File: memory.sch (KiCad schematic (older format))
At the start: 11 parts, among them U21 sst39x040, U22 generic_2048x8_TSOP_II_44, U23 generic_2048x8_TSOP_II_44, U24 generic_2048x8_TSOP_II_44, U25 generic_2048x8_TSOP_II_44

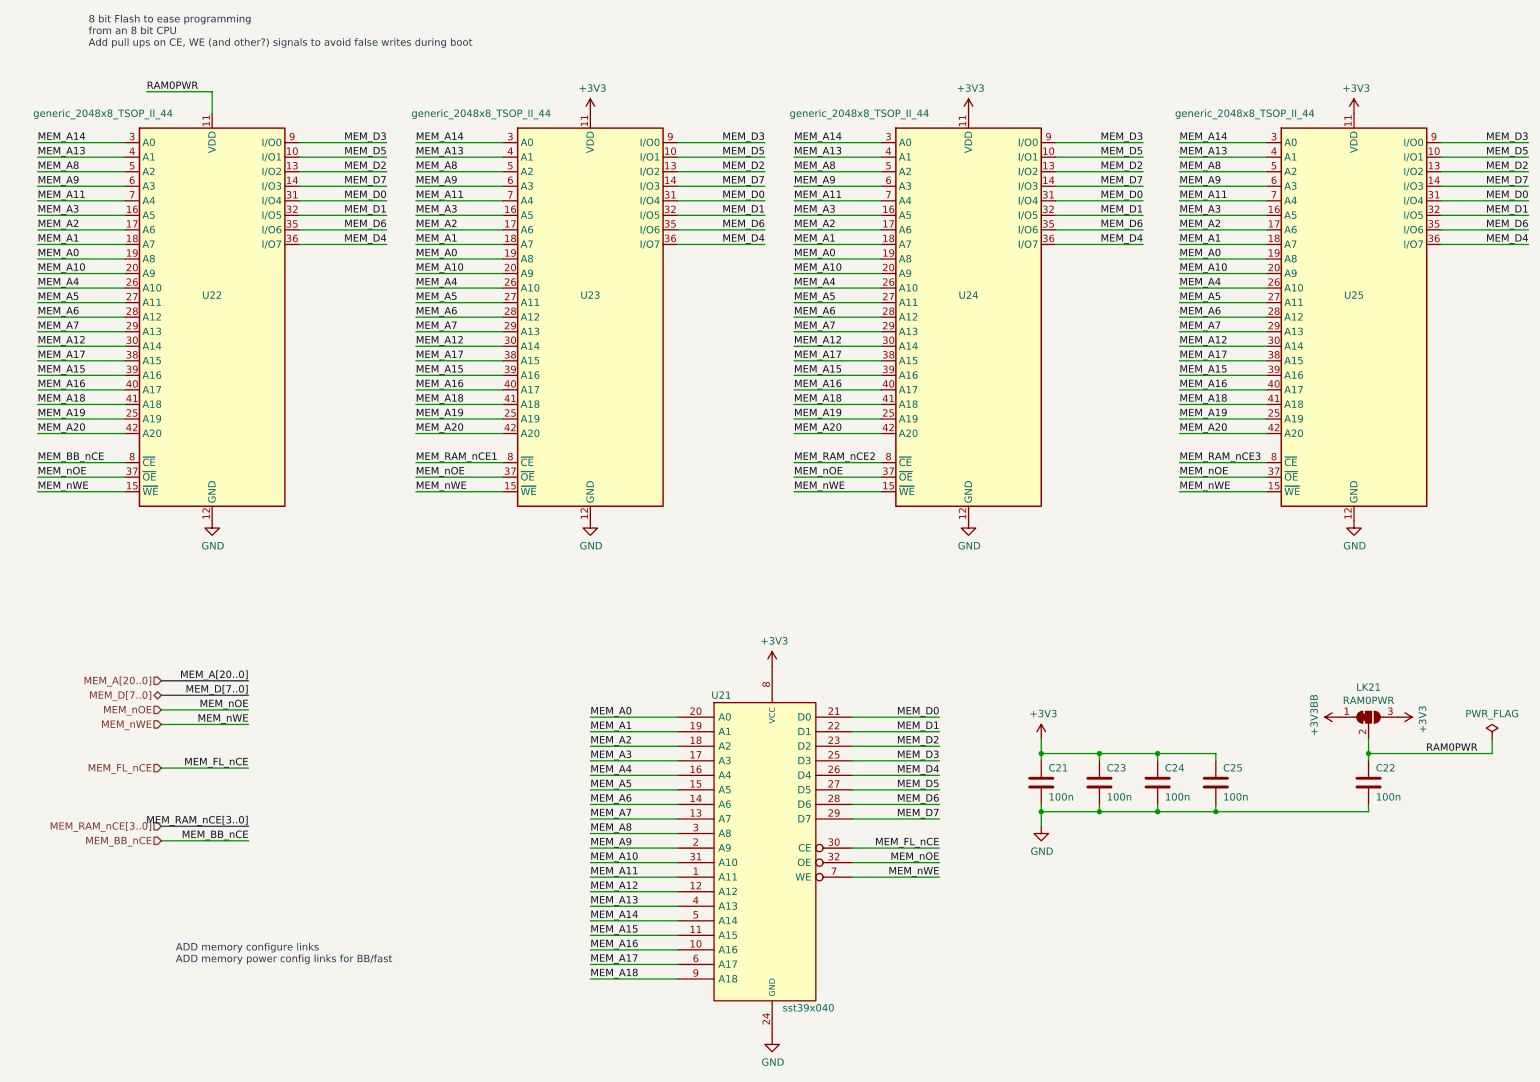
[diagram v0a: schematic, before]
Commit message: Mk.3 fixes and new 68000 expansion board
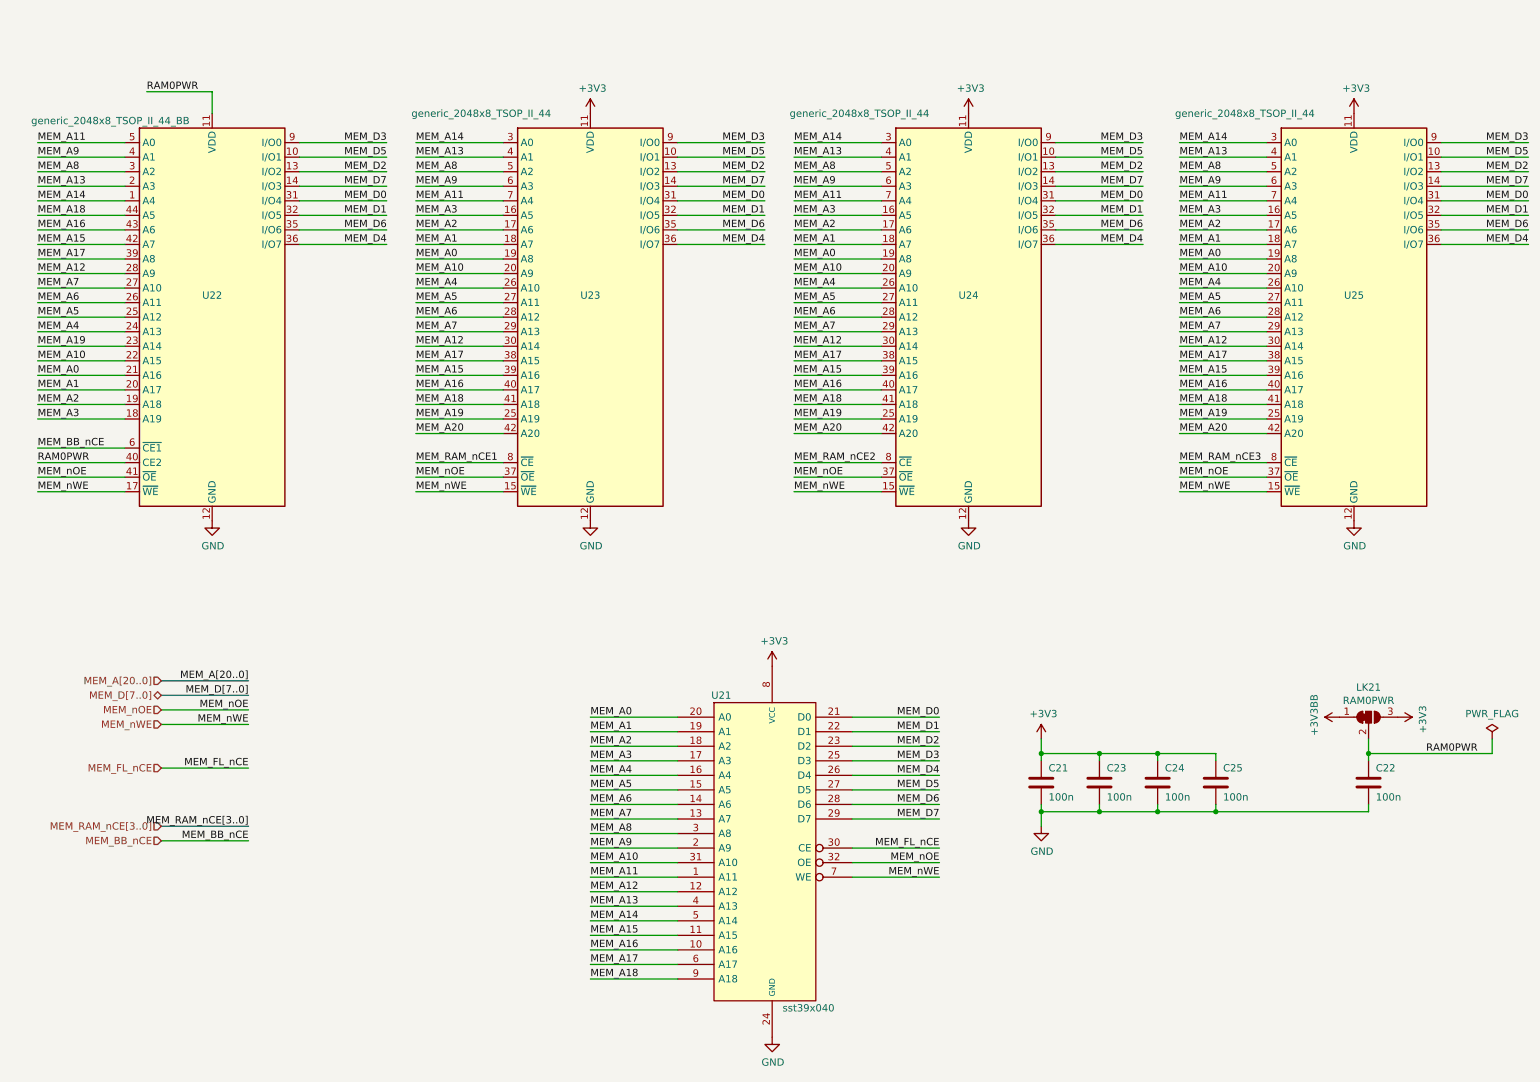
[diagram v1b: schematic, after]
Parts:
- removed U22: generic_2048x8_TSOP_II_44, Package_SO:TSOP-II-44_10.16x18.41mm_P0.8mm, symbol memory:generic_2048x8_TSOP_II_44
- added U22: generic_2048x8_TSOP_II_44_BB, Package_SO:TSOP-II-44_10.16x18.41mm_P0.8mm, symbol memory:generic_2048x8_TSOP_II_44_BB
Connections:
- net GND: now also U22.12 (GND), U22.34 (GND)
- net MEM_A0: now also U22.21 (A16)
- net MEM_A1: now also U22.20 (A17)
- net MEM_A10: now also U22.22 (A15)
- net MEM_A11: now also U22.5 (A0)
- net MEM_A12: now also U22.28 (A9)
- net MEM_A13: now also U22.2 (A3)
- net MEM_A14: now also U22.1 (A4)
- net MEM_A15: now also U22.42 (A7)
- net MEM_A16: now also U22.43 (A6)
- net MEM_A17: now also U22.39 (A8)
- net MEM_A18: now also U22.44 (A5)
- net MEM_A19: now also U22.23 (A14)
- net MEM_A2: now also U22.19 (A18)
- net MEM_A3: now also U22.18 (A19)
- net MEM_A4: now also U22.24 (A13)
- net MEM_A5: now also U22.25 (A12)
- net MEM_A6: now also U22.26 (A11)
- net MEM_A7: now also U22.27 (A10)
- net MEM_A8: now also U22.3 (A2)
- net MEM_A9: now also U22.4 (A1)
- net MEM_BB_nCE: now also U22.6 (~CE1)
- net MEM_D0: now also U22.31 (I/O4)
- net MEM_D1: now also U22.32 (I/O5)
- net MEM_D2: now also U22.13 (I/O2)
- net MEM_D3: now also U22.9 (I/O0)
- net MEM_D4: now also U22.36 (I/O7)
- net MEM_D5: now also U22.10 (I/O1)
- net MEM_D6: now also U22.35 (I/O6)
- net MEM_D7: now also U22.14 (I/O3)
- net MEM_nOE: now also U22.41 (~OE)
- net MEM_nWE: now also U22.17 (~WE)
- net RAM0PWR: now also U22.11 (VDD), U22.33 (VDD), U22.40 (CE2)
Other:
- note removed: "8 bit Flash to ease programming\nfrom an 8 bit CPU\nAdd pull ups on CE, WE (and other?) signals to avoid false writes during boot"
- note removed: "ADD memory configure links\nADD memory power config links for BB/fast"
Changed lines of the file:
@@
 Sheet 3 11
 Title "Mk.3 Blitter FPGA development board"
-Date "2021-05-08"
-Rev "3.00"
+Date "2021-08-14"
+Rev "3.03"
 Comp "Dossytronics"
-Comment1 ""
+Comment1 "fixed: clk/sysd0, jtag, u22 footprint"
 Comment2 ""
 Comment3 ""
 Comment4 ""
 $EndDescr
-Text Notes 950  800  0    50   ~ 0
-8 bit Flash to ease programming\nfrom an 8 bit CPU\nAdd pull ups on CE, WE (and other?) signals to avoid false writes during boot
 $Comp
 L sst39:sst39x040 U21
@@
 Text Label 6800 6100 2    50   ~ 0
 MEM_D7
-Text Label 600  2150 0    50   ~ 0
+Text Label 600  3150 0    50   ~ 0
 MEM_A1
-Text Label 600  2050 0    50   ~ 0
+Text Label 600  3250 0    50   ~ 0
 MEM_A2
-Text Label 600  1950 0    50   ~ 0
+Text Label 600  3350 0    50   ~ 0
 MEM_A3
+Text Label 600  2750 0    50   ~ 0
+MEM_A4
+Text Label 600  2650 0    50   ~ 0
+MEM_A5
+Text Label 600  2550 0    50   ~ 0
+MEM_A6
 Text Label 600  2450 0    50   ~ 0
-MEM_A4
-Text Label 600  2550 0    50   ~ 0
-MEM_A5
-Text Label 600  2650 0    50   ~ 0
-MEM_A6
-Text Label 600  2750 0    50   ~ 0
 MEM_A7
 Text Label 600  1650 0    50   ~ 0
 MEM_A8
+Text Label 600  1550 0    50   ~ 0
+MEM_A9
+Text Label 600  2950 0    50   ~ 0
+MEM_A10
+Text Label 600  1450 0    50   ~ 0
+MEM_A11
+Text Label 600  2350 0    50   ~ 0
+MEM_A12
 Text Label 600  1750 0    50   ~ 0
-MEM_A9
-Text Label 600  2350 0    50   ~ 0
-MEM_A10
+MEM_A13
 Text Label 600  1850 0    50   ~ 0
-MEM_A11
-Text Label 600  2850 0    50   ~ 0
-MEM_A12
-Text Label 600  1550 0    50   ~ 0
-MEM_A13
-Text Label 600  1450 0    50   ~ 0
 MEM_A14
-Text Label 600  2950 0    50   ~ 0
+Text Label 600  2250 0    50   ~ 0
 MEM_A17
-Text Label 600  3250 0    50   ~ 0
+Text Label 600  1950 0    50   ~ 0
 MEM_A18
 Wire Wire Line
@@
 Wire Wire Line
 	600  3350 1200 3350
-Wire Wire Line
-	600  3450 1200 3450
-Text Label 600  3350 0    50   ~ 0
+Text Label 600  2850 0    50   ~ 0
 MEM_A19
-Text Label 600  3450 0    50   ~ 0
-MEM_A20
-Text Label 600  2250 0    50   ~ 0
+Text Label 600  3050 0    50   ~ 0
 MEM_A0
-Text Notes 1550 7100 0    50   ~ 0
-ADD memory configure links\nADD memory power config links for BB/fast
-$Comp
-L memory:generic_2048x8_TSOP_II_44 U22
-U 1 1 60D1BD24
-P 1800 2550
-F 0 "U22" H 1800 2600 50  0000 C CNN
-F 1 "generic_2048x8_TSOP_II_44" H 1050 3850 50  0000 C CNN
-F 2 "Package_SO:TSOP-II-44_10.16x18.41mm_P0.8mm" H 750 3900 50  0001 C CNN
-F 3 "http://www.issi.com/WW/pdf/61-64C5128AL.pdf" H 1800 2550 50  0001 C CNN
-	1    1800 2550
-	1    0    0    -1
-$EndComp
 $Comp
 L power:GND #PWR0138
@@
 Wire Wire Line
 	600  2950 1200 2950
-Text Label 600  3150 0    50   ~ 0
+Text Label 600  2050 0    50   ~ 0
 MEM_A16
-Text Label 600  3050 0    50   ~ 0
+Text Label 600  2150 0    50   ~ 0
 MEM_A15
 Text Label 3200 2150 0    50   ~ 0
@@
 Wire Wire Line
 	9750 5650 10600 5650
-Text Label 600  3650 0    50   ~ 0
+Text Label 600  3550 0    50   ~ 0
 MEM_BB_nCE
 Text Label 2050 6250 2    50   ~ 0
@@
 Text HLabel 1450 6250 0    50   Input ~ 0
 MEM_BB_nCE
+$Comp
+L memory:generic_2048x8_TSOP_II_44_BB U22
+U 1 1 61191FA2
+P 1800 2550
+F 0 "U22" H 1800 2600 50  0000 C CNN
+F 1 "generic_2048x8_TSOP_II_44_BB" H 1100 3800 50  0000 C CNN
+F 2 "Package_SO:TSOP-II-44_10.16x18.41mm_P0.8mm" H 750 3900 50  0001 C CNN
+F 3 "http://www.issi.com/WW/pdf/61-64C5128AL.pdf" H 1800 2550 50  0001 C CNN
+	1    1800 2550
+	1    0    0    -1
+$EndComp
+Wire Wire Line
+	1200 3550 600  3550
+Text Label 600  3650 0    50   ~ 0
+RAM0PWR
 $EndSCHEMATC
